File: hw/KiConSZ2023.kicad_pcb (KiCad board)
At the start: 4 copper layers, 100 x 60 mm, 110 parts, among them J2 Conn_01x06, J3 USB_C_Receptacle_USB2.0, J4 Conn_02x03_Top_Bottom, J5 Conn_02x03_Top_Bottom, J6 BM20B(0.8)-10DS-0.4V, Q10 SK2302AAT, Q11 SK2302AAT, Q12 SK2302AAT, Q13 SK2302AAT, Q14 SK2302AAT, Q15 SK2302AAT, Q16 SK2302AAT, Q17 SK2302AAT, Q2 SK2302AAT, Q3 SK2302AAT, Q4 SK2302AAT, Q5 SK2302AAT, Q6 SK2302AAT, Q7 SK2302AAT, Q8 SK2302AAT, Q9 SK2302AAT, SW2 SKRPACE010, SW3 SKRPACE010, SW4 SW_SPDT, U2 N32L406RBL7, U3 PUSB3FR4, U4 SY8088IAAC, U5 ME2118C33M5G

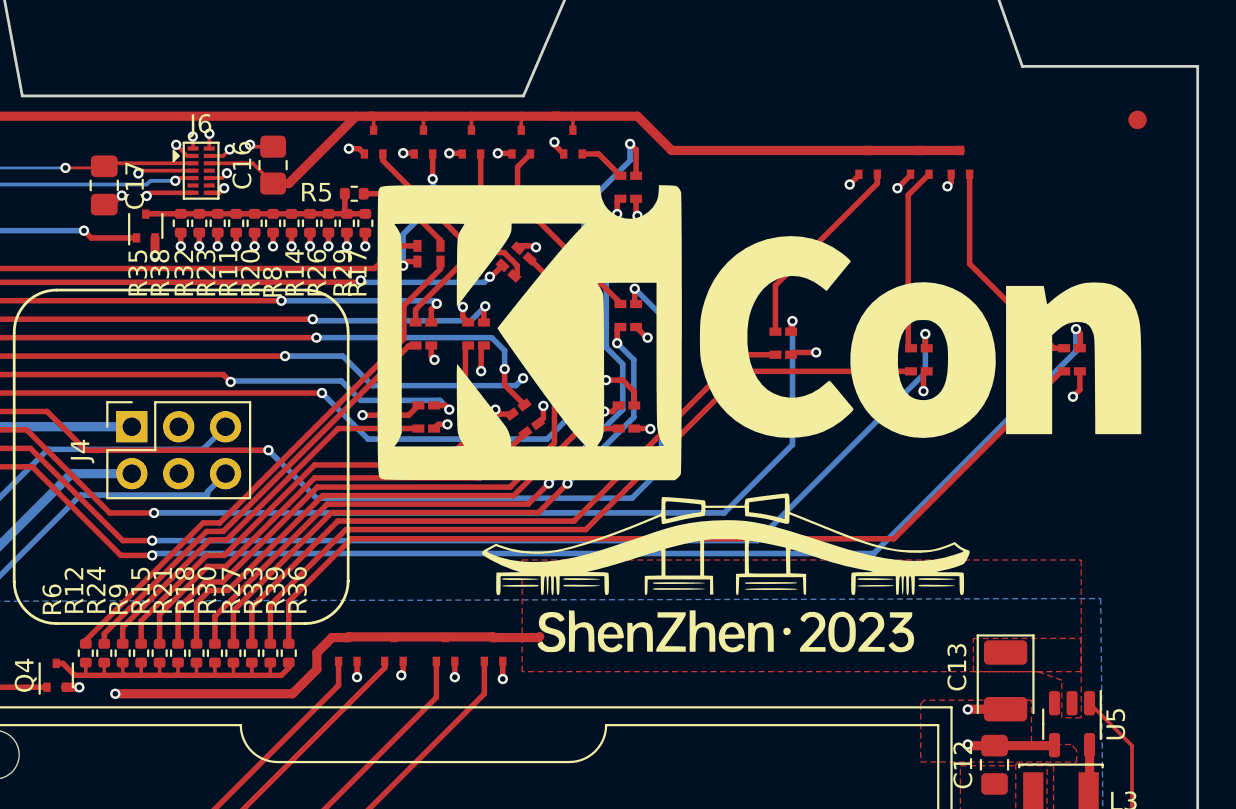
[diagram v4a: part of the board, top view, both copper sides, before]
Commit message: added SMT Marks; fix DFMs
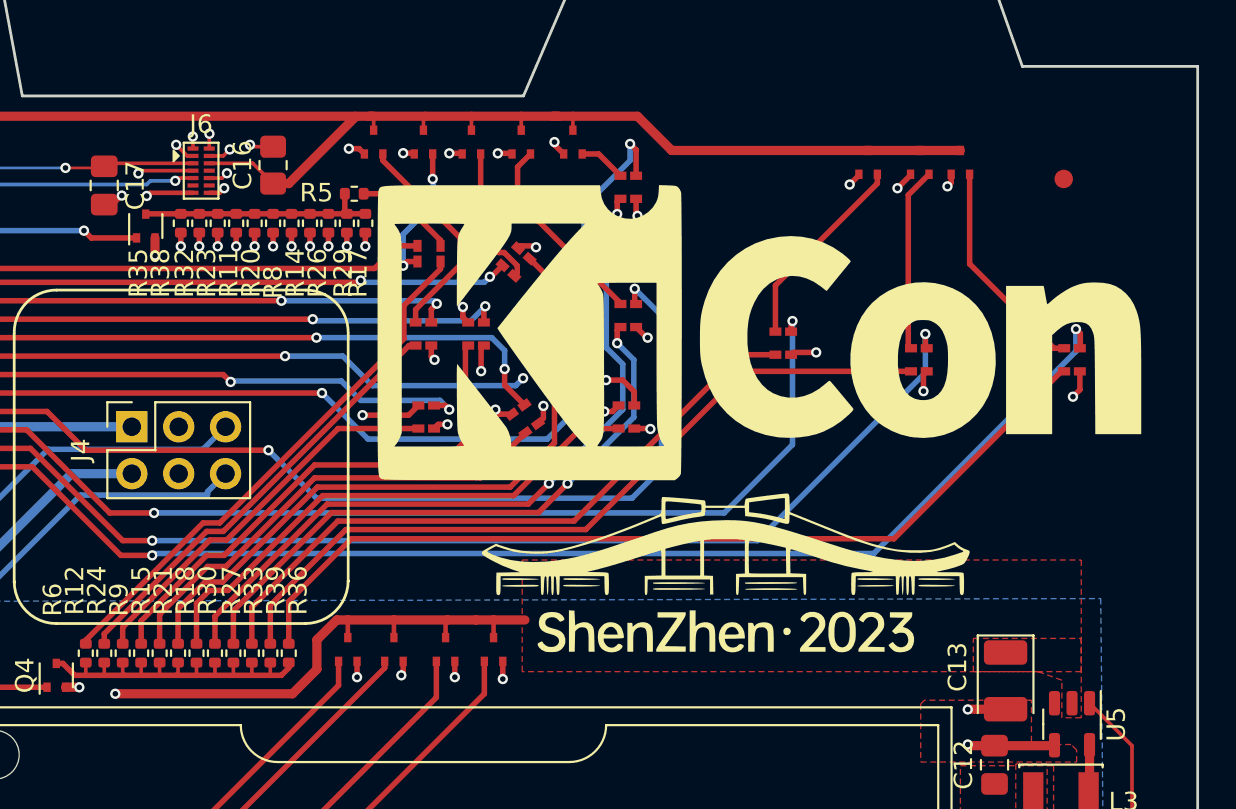
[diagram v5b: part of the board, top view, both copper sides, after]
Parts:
- moved MK2 5.12 mm to (143.0, 93.7)
- renumbered REF** to MK1, REF** to MK2
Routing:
- net VDDA: track 271.8 -> 275.6 mm
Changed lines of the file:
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@@
   )
   (footprint "IotPi_TestPoints_Marks:SMT_Mark" (layer "F.Cu")
-    (at 147 90.5)
+    (at 143 93.7)
     (attr board_only exclude_from_bom)
-    (fp_text reference "REF**" (at 0 -0.5 unlocked) (layer "F.SilkS") hide
+    (fp_text reference "MK2" (at -3.5 -0.7 unlocked) (layer "F.Fab")
         (effects (font (size 1 1) (thickness 0.1)))
     )
@@
     (at 57.8 120.6)
     (attr board_only exclude_from_bom)
-    (fp_text reference "REF**" (at 0 -0.5 unlocked) (layer "F.SilkS") hide
+    (fp_text reference "MK1" (at 0 -0.5 unlocked) (layer "F.Fab")
         (effects (font (size 1 1) (thickness 0.1)))
     )
@@
   (segment (start 64.65 110.45) (end 66.2 112) (width 0.5) (layer "F.Cu") (net 121))
   (segment (start 73.9 92.85) (end 75.7 94.65) (width 0.5) (layer "F.Cu") (net 121))
-  (segment (start 104.2 118.555) (end 103.345 118.555) (width 0.5) (layer "F.Cu") (net 121))
   (segment (start 75.7 95) (end 75.7 101.15) (width 0.5) (layer "F.Cu") (net 121))
   (segment (start 113.6 90.3) (end 110.9 90.3) (width 0.5) (layer "F.Cu") (net 121))
+  (segment (start 112.1 117.6) (end 113.8 117.6) (width 0.5) (layer "F.Cu") (net 121))
   (segment (start 73.7125 123.95) (end 74.6 123.0625) (width 0.3) (layer "F.Cu") (net 121))
-  (segment (start 102.525 119.375) (end 102.525 120.275) (width 0.5) (layer "F.Cu") (net 121))
   (segment (start 99.05 92.85) (end 100.15 93.95) (width 0.2) (layer "F.Cu") (net 121))
+  (segment (start 91.6 121.6) (end 101.2 121.6) (width 0.5) (layer "F.Cu") (net 121))
   (segment (start 60.9625 118.1125) (end 60.95 118.1) (width 0.5) (layer "F.Cu") (net 121))
   (segment (start 60.825 131.45) (end 59.4875 131.45) (width 0.3) (layer "F.Cu") (net 121))
   (segment (start 68.75 133.375) (end 68.75 136.0125) (width 0.3) (layer "F.Cu") (net 121))
-  (segment (start 112.1 118.555) (end 114.545 118.555) (width 0.5) (layer "F.Cu") (net 121))
+  (segment (start 102.525 118.675) (end 103.6 117.6) (width 0.5) (layer "F.Cu") (net 121))
   (segment (start 64.8 109.55) (end 64.65 109.7) (width 0.5) (layer "F.Cu") (net 121))
-  (segment (start 102.525 120.275) (end 101.2 121.6) (width 0.5) (layer "F.Cu") (net 121))
   (segment (start 72.175 130.45) (end 74.7125 130.45) (width 0.3) (layer "F.Cu") (net 121))
   (segment (start 59.4875 131.45) (end 58.7 132.2375) (width 0.3) (layer "F.Cu") (net 121))
@@
   (segment (start 105.6 90.3) (end 81.6 90.3) (width 0.5) (layer "F.Cu") (net 121))
   (segment (start 52.2 118.15) (end 59.2125 118.15) (width 0.5) (layer "F.Cu") (net 121))
-  (segment (start 101.2 121.6) (end 91.6 121.6) (width 0.5) (layer "F.Cu") (net 121))
   (segment (start 81.6 90.3) (end 76.9 95) (width 0.5) (layer "F.Cu") (net 121))
   (segment (start 132.4 92.155) (end 137.4 92.155) (width 0.5) (layer "F.Cu") (net 121))
   (segment (start 121.755 92.155) (end 132.4 92.155) (width 0.5) (layer "F.Cu") (net 121))
+  (segment (start 109.5 117.7) (end 109.6 117.6) (width 0.25) (layer "F.Cu") (net 121))
   (segment (start 72.1 113.4) (end 72.075 113.425) (width 0.2) (layer "F.Cu") (net 121))
   (segment (start 119.9 90.3) (end 121.755 92.155) (width 0.5) (layer "F.Cu") (net 121))
@@
   (segment (start 72.075 113.425) (end 67.925 113.425) (width 0.3) (layer "F.Cu") (net 121))
   (segment (start 101 93.95) (end 104.6 90.35) (width 0.5) (layer "F.Cu") (net 121))
+  (segment (start 109.6 117.6) (end 111.145 117.6) (width 0.5) (layer "F.Cu") (net 121))
   (segment (start 76.9 95) (end 75.7 95) (width 0.5) (layer "F.Cu") (net 121))
   (segment (start 74.7125 130.45) (end 74.9 130.2625) (width 0.3) (layer "F.Cu") (net 121))
+  (segment (start 104.2 118.555) (end 104.2 117.6) (width 0.25) (layer "F.Cu") (net 121))
   (segment (start 58.7 132.2375) (end 58.7 135.1) (width 0.2) (layer "F.Cu") (net 121))
   (segment (start 75.6875 108.7625) (end 75.6875 106.9) (width 0.5) (layer "F.Cu") (net 121))
   (segment (start 116.4 91.055) (end 116.4 90.3) (width 0.2) (layer "F.Cu") (net 121))
-  (segment (start 112.06 118.515) (end 104.24 118.515) (width 0.5) (layer "F.Cu") (net 121))
+  (segment (start 106.7 117.6) (end 109.6 117.6) (width 0.5) (layer "F.Cu") (net 121))
+  (segment (start 103.6 117.6) (end 104.2 117.6) (width 0.5) (layer "F.Cu") (net 121))
   (segment (start 72.175 123.95) (end 73.7125 123.95) (width 0.3) (layer "F.Cu") (net 121))
   (segment (start 108.3 90.4) (end 108.4 90.3) (width 0.2) (layer "F.Cu") (net 121))
@@
   (segment (start 100.15 93.95) (end 101 93.95) (width 0.5) (layer "F.Cu") (net 121))
   (segment (start 69.3375 136.6) (end 71.1625 136.6) (width 0.5) (layer "F.Cu") (net 121))
+  (segment (start 102.525 120.275) (end 102.525 118.675) (width 0.5) (layer "F.Cu") (net 121))
+  (segment (start 106.7 118.555) (end 106.7 117.6) (width 0.25) (layer "F.Cu") (net 121))
+  (segment (start 112.1 118.555) (end 112.1 117.6) (width 0.25) (layer "F.Cu") (net 121))
   (segment (start 69.3375 138.7) (end 69.3375 136.6) (width 0.5) (layer "F.Cu") (net 121))
-  (segment (start 104.24 118.515) (end 104.2 118.555) (width 0.5) (layer "F.Cu") (net 121))
   (segment (start 68.75 133.375) (end 68.75 131.85) (width 0.3) (layer "F.Cu") (net 121))
   (segment (start 62.75 122.025) (end 62.75 121.6875) (width 0.3) (layer "F.Cu") (net 121))
@@
   (segment (start 64.65 109.7) (end 64.65 110.45) (width 0.5) (layer "F.Cu") (net 121))
   (segment (start 78.6 113.4) (end 72.1 113.4) (width 0.2) (layer "F.Cu") (net 121))
+  (segment (start 111.145 117.6) (end 112.1 117.6) (width 0.5) (layer "F.Cu") (net 121))
   (segment (start 58.7 135.1) (end 59.6 136) (width 0.2) (layer "F.Cu") (net 121))
   (segment (start 108.4 90.3) (end 105.355 90.3) (width 0.5) (layer "F.Cu") (net 121))
   (segment (start 113.6 91.055) (end 113.6 90.3) (width 0.2) (layer "F.Cu") (net 121))
   (segment (start 104.6 90.35) (end 104.6 90.3) (width 0.5) (layer "F.Cu") (net 121))
-  (segment (start 112.1 118.555) (end 112.06 118.515) (width 0.5) (layer "F.Cu") (net 121))
   (segment (start 74.9 130.2625) (end 74.9 131.2) (width 0.3) (layer "F.Cu") (net 121))
   (segment (start 116.4 90.3) (end 119.9 90.3) (width 0.5) (layer "F.Cu") (net 121))
@@
   (segment (start 72.45 112) (end 75.6875 108.7625) (width 0.5) (layer "F.Cu") (net 121))
   (segment (start 96.69 92.85) (end 99.05 92.85) (width 0.2) (layer "F.Cu") (net 121))
+  (segment (start 109.5 118.555) (end 109.5 117.7) (width 0.25) (layer "F.Cu") (net 121))
   (segment (start 115.645 90.3) (end 113.6 90.3) (width 0.5) (layer "F.Cu") (net 121))
   (segment (start 110.9 90.3) (end 108.4 90.3) (width 0.5) (layer "F.Cu") (net 121))
+  (segment (start 101.2 121.6) (end 102.525 120.275) (width 0.5) (layer "F.Cu") (net 121))
   (segment (start 78.925 113.725) (end 78.6 113.4) (width 0.2) (layer "F.Cu") (net 121))
-  (segment (start 103.345 118.555) (end 102.525 119.375) (width 0.5) (layer "F.Cu") (net 121))
   (segment (start 64.8 107.6) (end 64.8 109.55) (width 0.5) (layer "F.Cu") (net 121))
-  (segment (start 114.545 118.555) (end 114.6 118.5) (width 0.5) (layer "F.Cu") (net 121))
   (segment (start 68.75 136.0125) (end 69.3375 136.6) (width 0.3) (layer "F.Cu") (net 121))
+  (segment (start 104.2 117.6) (end 106.7 117.6) (width 0.5) (layer "F.Cu") (net 121))
   (via (at 78.5 120.5) (size 0.56) (drill 0.3) (layers "F.Cu" "B.Cu") (net 121))
   (via (at 79.4 124.1) (size 0.56) (drill 0.3) (layers "F.Cu" "B.Cu") (net 121))

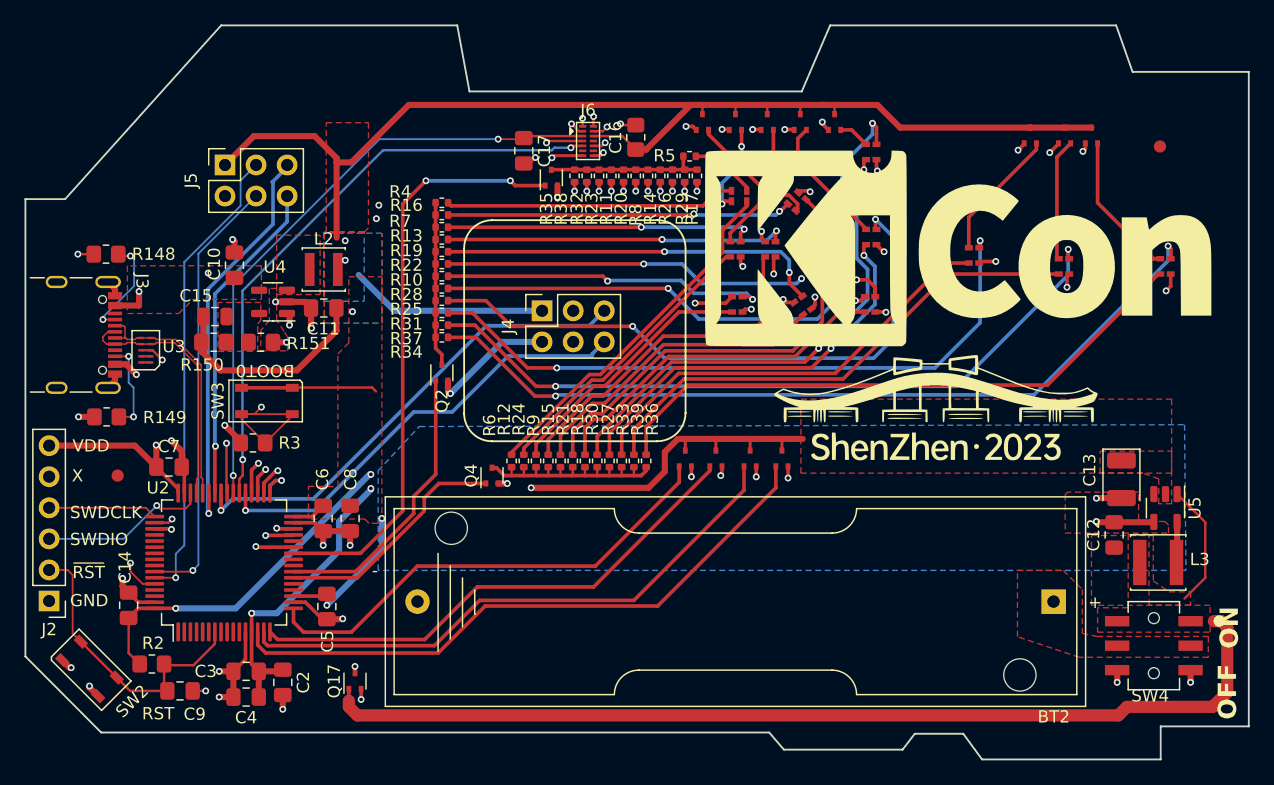
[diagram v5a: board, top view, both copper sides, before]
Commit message: fix footprint of BM20B(x)-10DS-0.4V
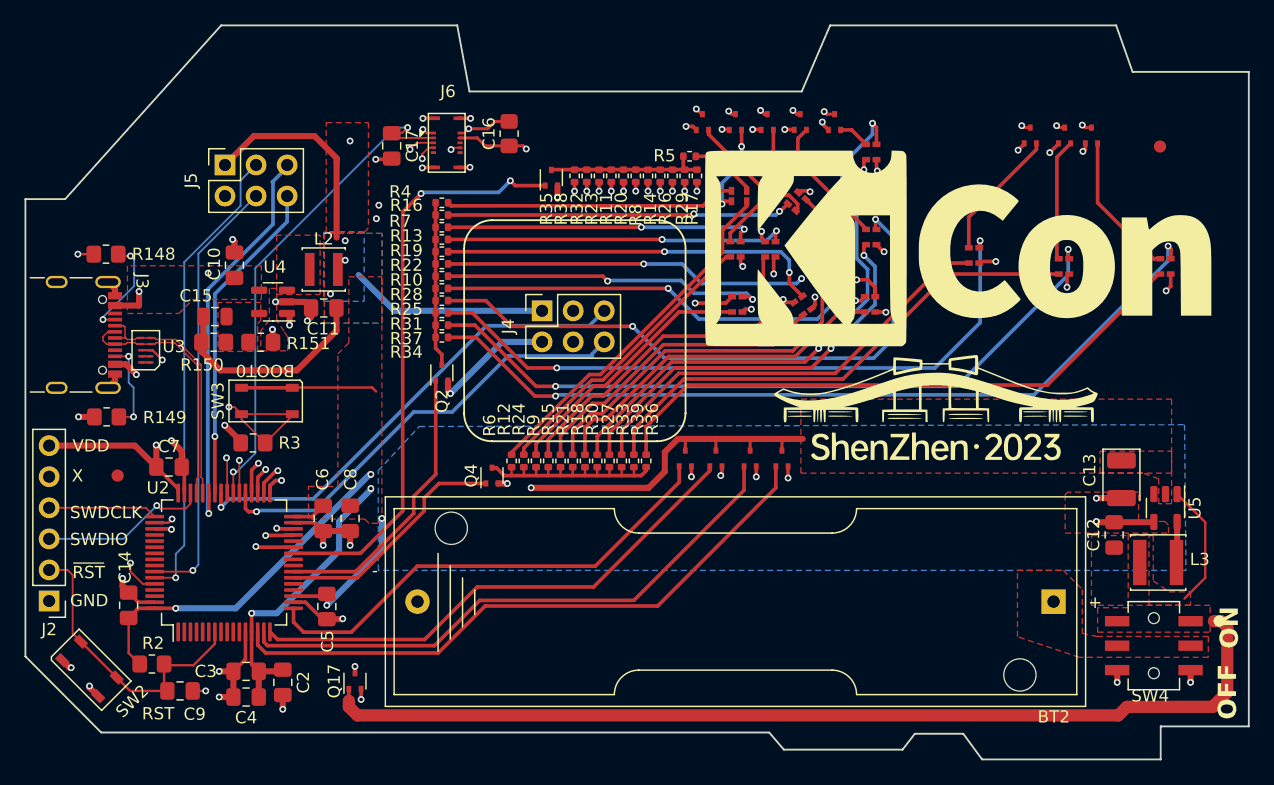
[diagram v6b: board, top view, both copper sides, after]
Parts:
- J6: value BM20B(0.8)-10DS-0.4V -> BM20B(0.6)-10DS-0.4V; footprint IotPi_Connector_Hirose:BM20B(0.8)-10DS-0.4V -> IotPi_Connector_Hirose:BM20B(x)-10DS-0.4V
- moved J6 11.6 mm to (84.7, 93.4)
- moved C17 10.8 mm to (80.2, 93.7)
- moved C16 10.4 mm to (89.8, 92.7)
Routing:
- net /DISP_SCK: track 49.4 -> 35.0 mm
- net /DISP_MOSI: track 48.4 -> 38.0 mm
- net /DISP_DISP: track 50.6 -> 41.6 mm
- net /DISP_~{SS}: track 48.7 -> 42.5 mm
- net Net-(D12-GK): track 60.8 -> 58.9 mm
- net /MCU/BOOT0: track 32.7 -> 31.0 mm
- net VDDA: track 275.6 -> 275.8 mm, vias 11 -> 21
- net GND: track 81.6 -> 81.4 mm, vias 35 -> 34

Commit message: updated orientation of XL-1615RGBC
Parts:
- turned D10 to 90 degrees
- turned D11 to 90 degrees
- turned D12 to 90 degrees
- turned D13 to 90 degrees
- turned D2 to 180 degrees
- turned D3 to 90 degrees
- turned D4 to 90 degrees
- turned D5 to 90 degrees
- turned D6 to -132 degrees
- turned D7 to 126 degrees
- turned D8 to 90 degrees
- turned D9 to 90 degrees
